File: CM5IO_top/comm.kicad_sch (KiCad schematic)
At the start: 17 parts, among them J4 J_ESP_DBG_UART, SW1 SW_RESET, SW2 SW_BOOT, U1 ESP32-S3-WROOM-1, U4 Waveshare Core1262 SX1262

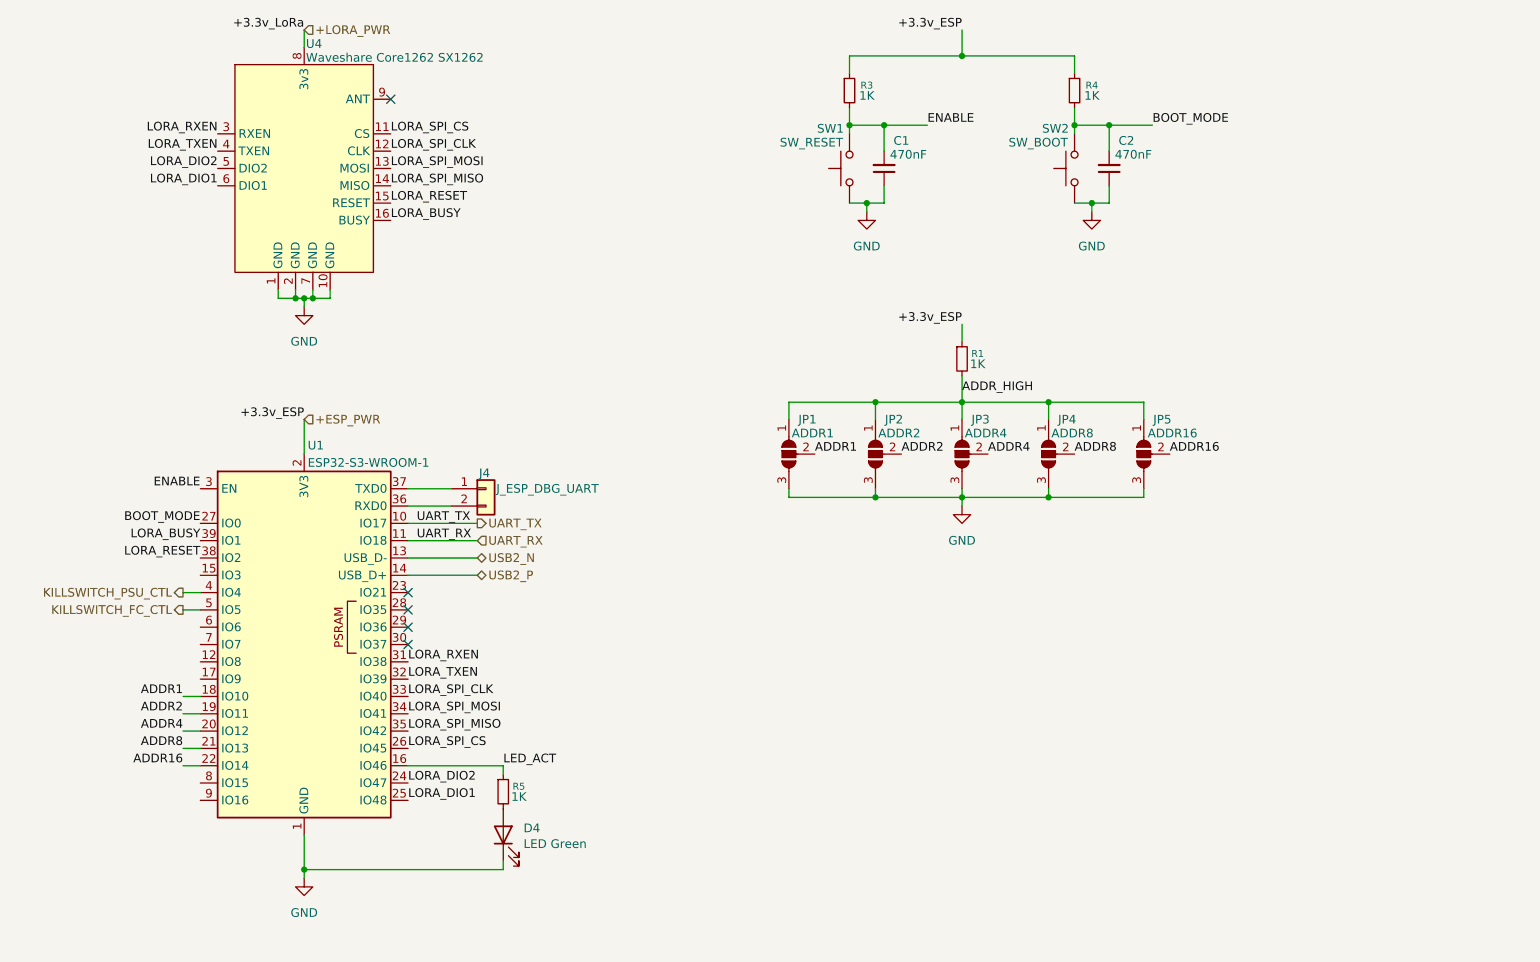
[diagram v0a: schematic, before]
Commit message: redesigning upper board
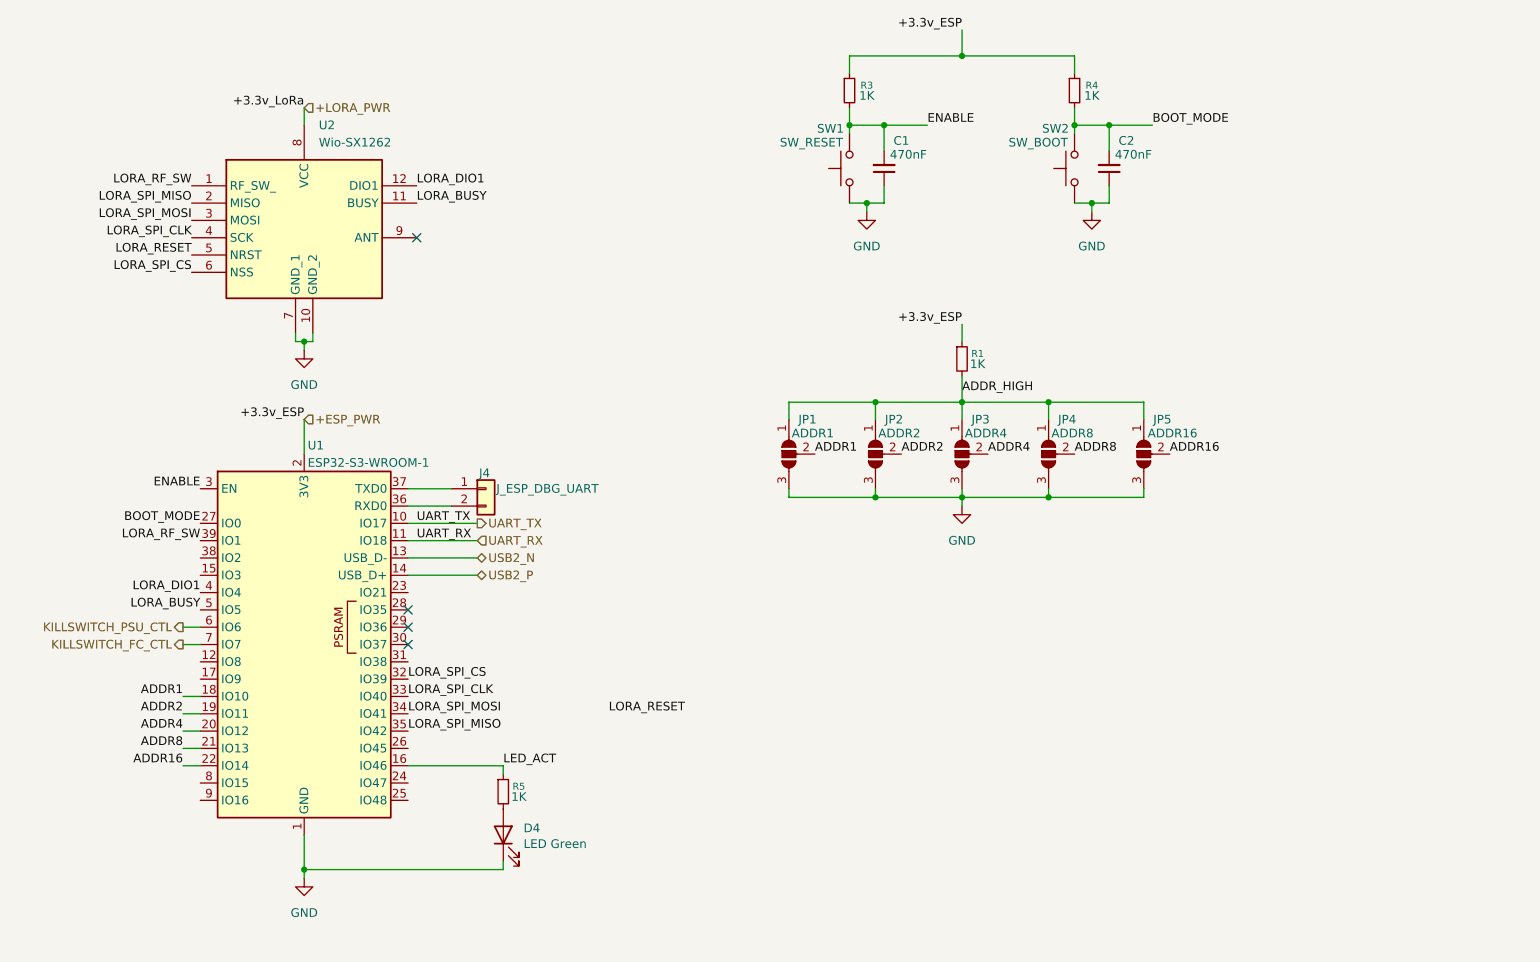
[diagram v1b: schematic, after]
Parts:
- removed U4: Waveshare Core1262 SX1262, CM5IO_top:Core1262_SX1262, symbol CM5IO:Core1262_SX1262
- added U2: Wio-SX1262, CM5IO_top:Wio-SX1262, symbol CM5IO:Wio-SX1262
- U1: footprint RF_Module:ESP32-S3-WROOM-1 -> RF_Module:ESP32-S3-WROOM-1U
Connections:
- net LORA_TXEN is gone; now on net LORA_SPI_CS: U1.32 (IO39)
- net +LORA_PWR: now also U2.8 (VCC)
- net GND: now also U2.10 (GND_2), U2.7 (GND_1)
- net KILLSWITCH_FC_CTL: now also U1.7 (IO7); no longer U1.5 (IO5)
- net KILLSWITCH_PSU_CTL: now also U1.6 (IO6); no longer U1.4 (IO4)
- net LORA_BUSY: now also U1.5 (IO5), U2.11 (BUSY); no longer U1.39 (IO1)
- net LORA_DIO1: now also U1.4 (IO4), U2.12 (DIO1); no longer U1.25 (IO48)
- net LORA_RESET: now also U2.5 (NRST); no longer U1.38 (IO2)
- net LORA_SPI_CLK: now also U2.4 (SCK)
- net LORA_SPI_CS: now also U2.6 (NSS); no longer U1.26 (IO45)
- net LORA_SPI_MISO: now also U2.2 (MISO)
- net LORA_SPI_MOSI: now also U2.3 (MOSI)
- net LORA_DIO2: no longer names the net of U1.24 (IO47)
- net LORA_RXEN: no longer names the net of U1.31 (IO38)
- new net LORA_RF_SW: U1.39 (IO1), U2.1 (RF_SW_)
- no-connect marks 5 -> 4

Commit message: upper board finished (I hope)
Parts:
- added C7, C8: 470nF, Capacitor_SMD:C_0805_2012Metric_Pad1.18x1.45mm_HandSolder, symbol Device:C_Small
- J4: footprint Connector_Molex:Molex_PicoBlade_53047-0210_1x02_P1.25mm_Vertical -> Connector_Molex:Molex_PicoBlade_53047-0310_1x03_P1.25mm_Vertical; symbol Connector_Generic:Conn_01x02 -> Connector_Generic:Conn_01x03; Field4 Farnell -> (none); Field5 9733051 -> (none); Field6 53047-0210 -> 53047-0310
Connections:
- net +ESP_PWR: now also C7.2
- net +LORA_PWR: now also C8.2
- net GND: now also J4.1 (Pin_1), C7.1, C8.1
- net KILLSWITCH_FC_CTL: now also U1.39 (IO1); no longer U1.7 (IO7)
- net LED_ACT: now also U1.26 (IO45); no longer U1.16 (IO46)
- net LORA_RESET: now also U1.32 (IO39)
- net LORA_RF_SW: now also U1.38 (IO2); no longer U1.39 (IO1)
- net LORA_SPI_CS: now also U1.31 (IO38); no longer U1.32 (IO39)
- net at U1.37 (TXD0): now also J4.2 (Pin_2); no longer J4.1 (Pin_1)
- net at U1.36 (RXD0): now also J4.3 (Pin_3); no longer J4.2 (Pin_2)
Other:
- moved on the sheet: C1, C2, D4, JP1, JP2, JP3, JP4, JP5, R1, R3, R4, R5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
